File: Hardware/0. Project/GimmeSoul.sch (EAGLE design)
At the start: 24 parts, among them CN1 2.1MMJACKTHM, U1 ATMEGA328P-AU, U2 REG1117-5.0

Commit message: Jumpers on PCB layout bug fix
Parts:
- added SJ2: (no value), jumper:SJ
- SJ1: device jumper:SJ2W -> jumper:SJ
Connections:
- new net N$6: JP1.3, SJ1.2
- net +5V: no longer JP1.2
- net ICSP_RESET: now also SJ2.1; no longer SJ1.3
- net N$5: now also SJ2.2; no longer SJ1.2
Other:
- note added: "DC Power Jack J4"
- note added: "On the first use of the GimmeSoul (U1 bootloader programing): SJ1 = OPEN SJ2 = CLOSE After, SJ1 = CLOSE SJ2 = OPEN"
- note removed: "SJ1 - Position 2-1: Position for conventional use of GimmeSoul. This position allows you to standalone programming the bootloader of other ATmega."
- note removed: "SJ1 - Position 2-3: On the first use of the GimmeSoul, this position allows you to programming the U1 bootloader using an Arduino UNO."
- moved on the sheet: CN1

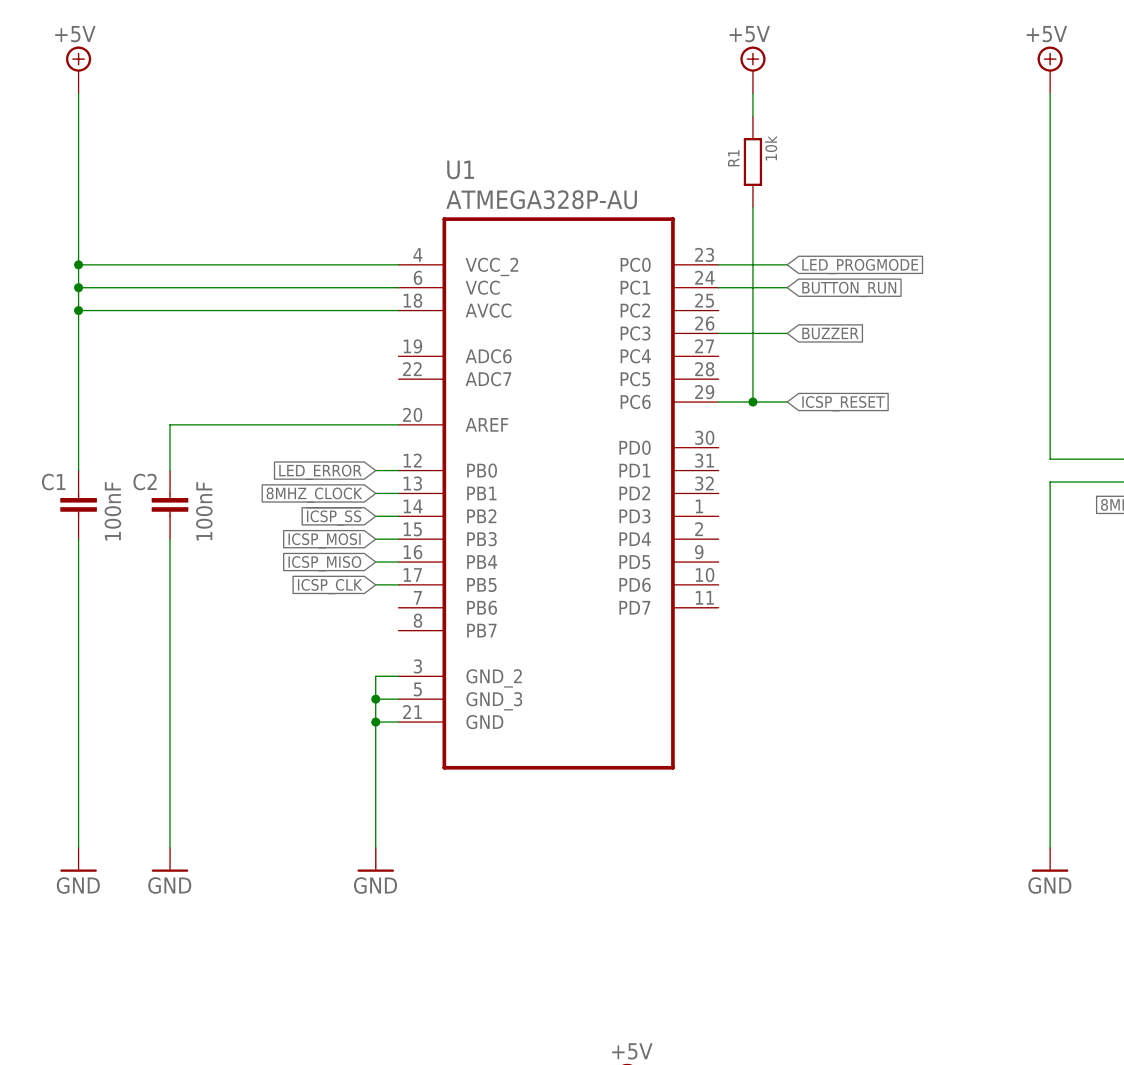
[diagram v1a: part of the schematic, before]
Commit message: 16MHz crystal added to MCU
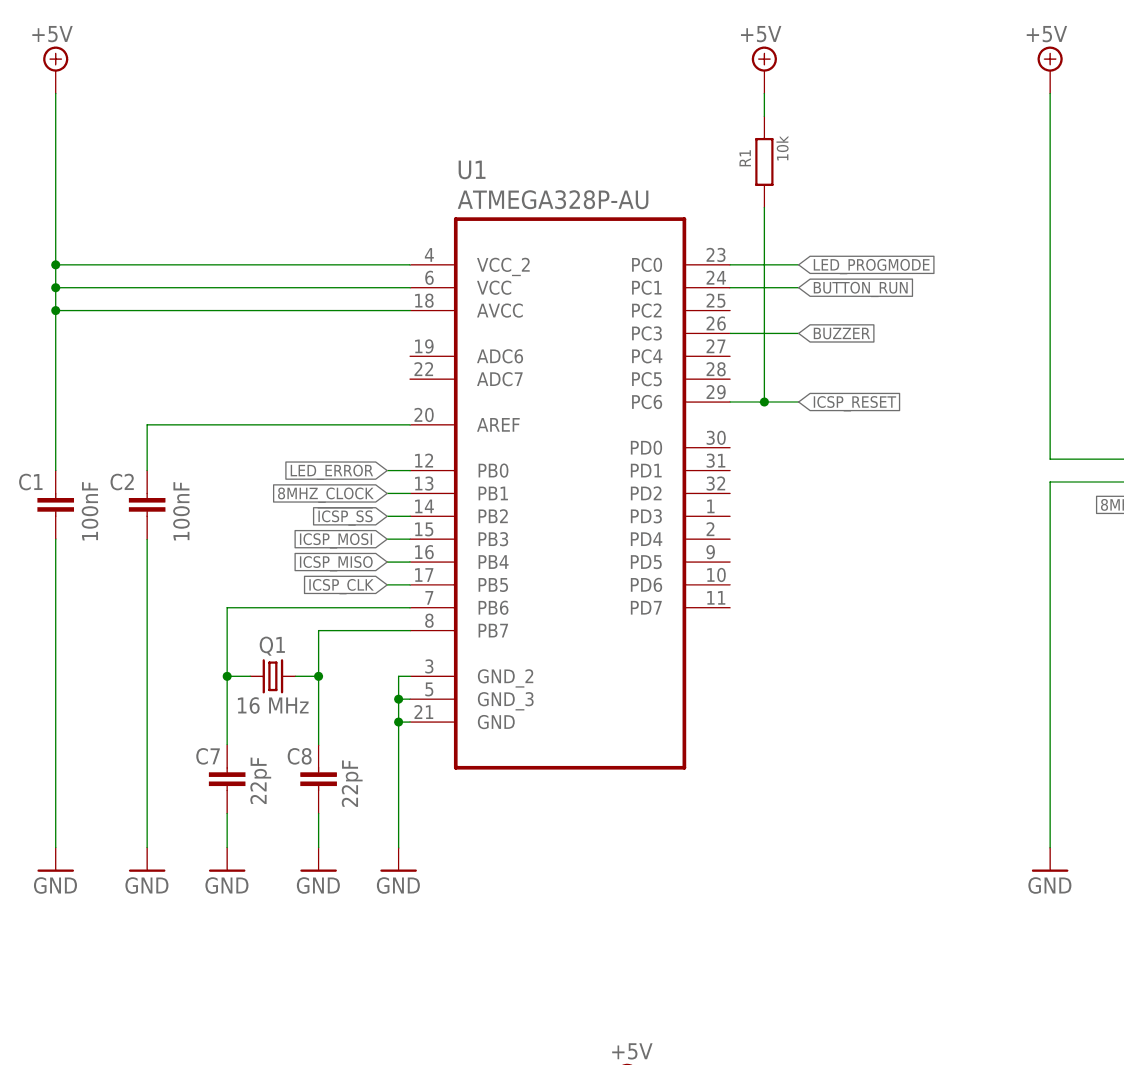
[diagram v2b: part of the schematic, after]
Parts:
- added C7, C8: 22pF, rcl:C-EUC0805
- added Q1: 16 MHz, crystal:CRYSTALHC49S
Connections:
- new net N$7: C7.2, Q1.1, U1.PB6
- new net N$8: C8.2, Q1.2, U1.PB7
- net GND: now also C7.1, C8.1
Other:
- moved on the sheet: C1, C2, R1, U1

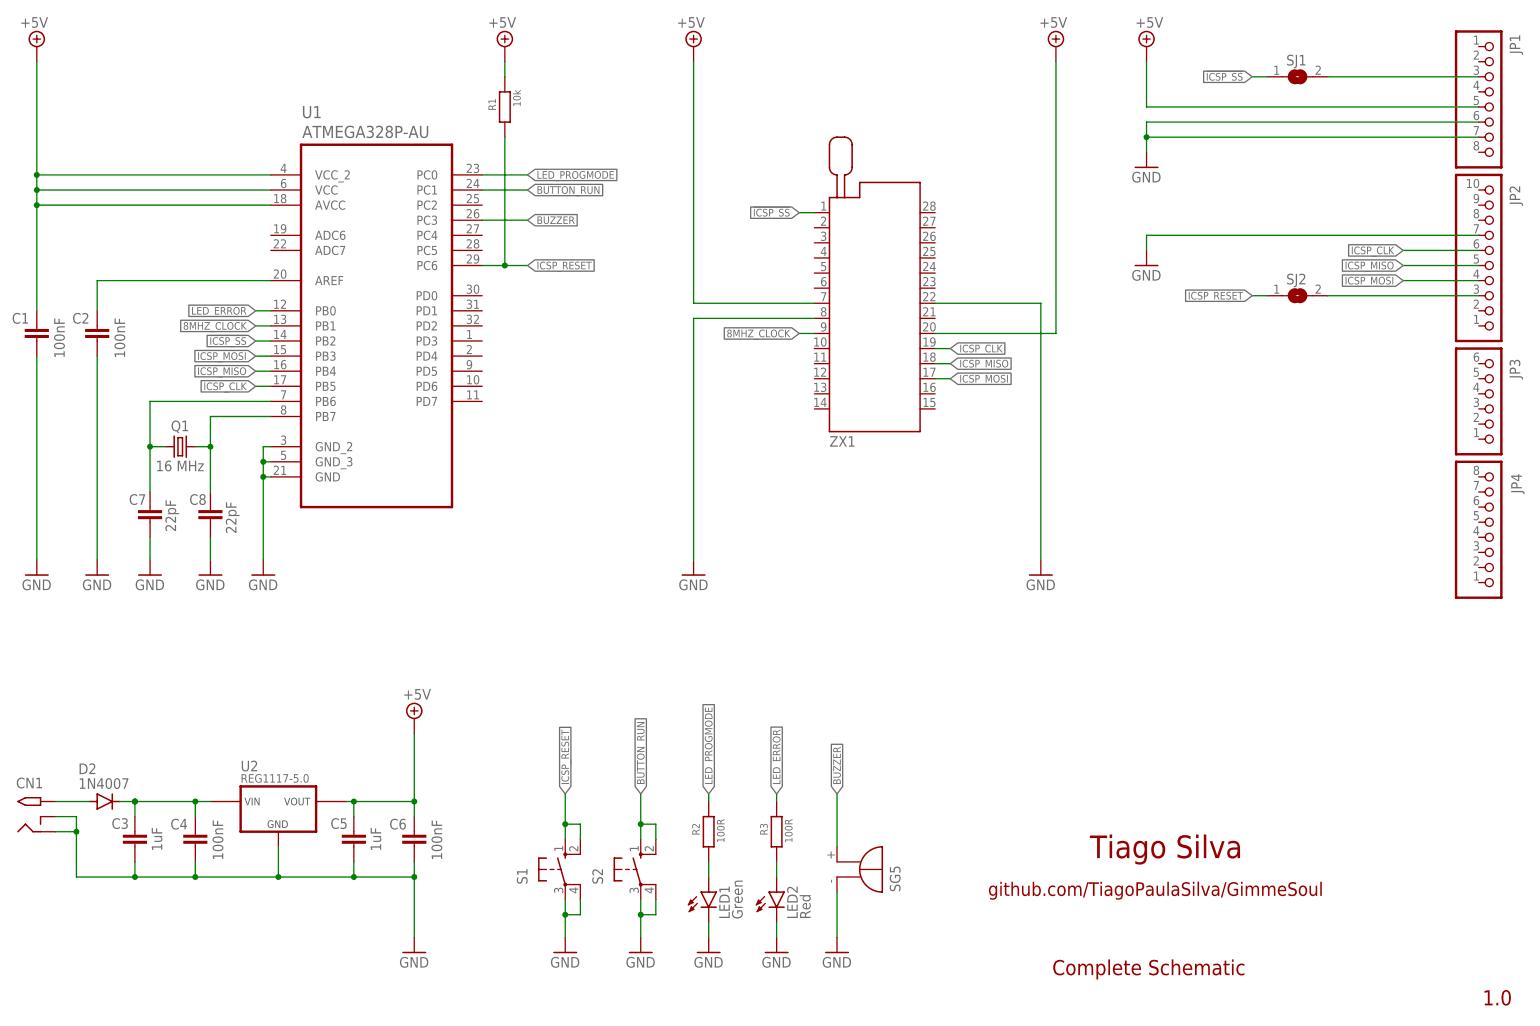
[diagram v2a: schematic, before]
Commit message: Silk Screen ref generated
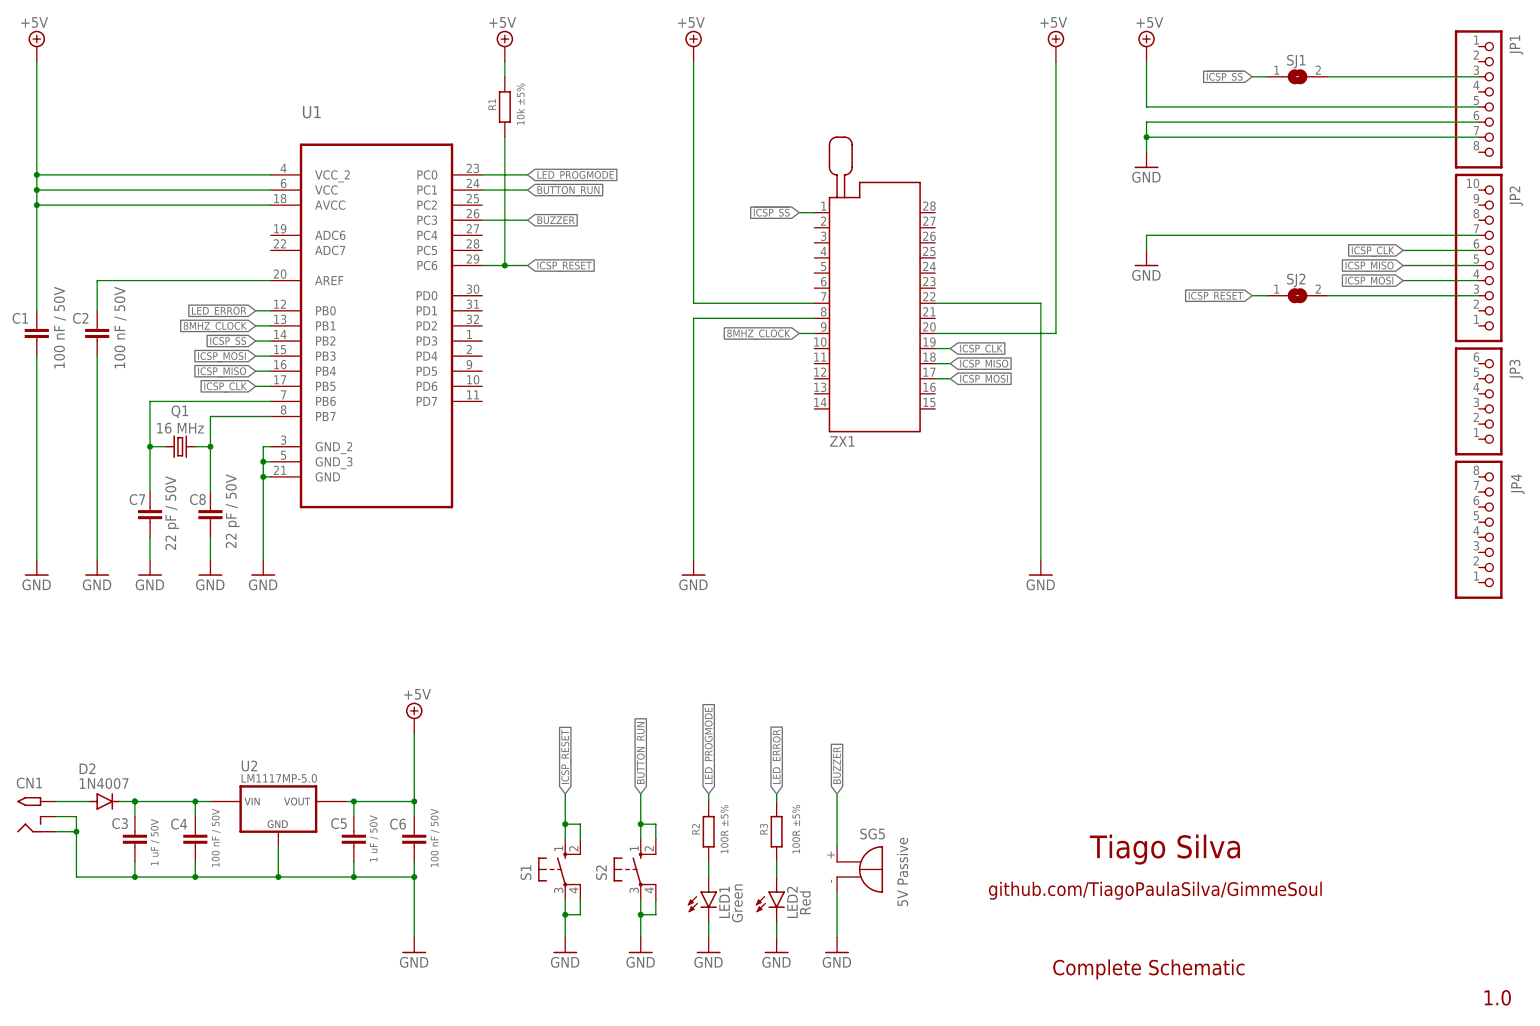
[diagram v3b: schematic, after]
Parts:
- C1, C2, C4, C6: value 100nF -> 100 nF / 50V
- C3, C5: value 1uF -> 1 uF / 50V
- C7, C8: value 22pF -> 22 pF / 50V
- R1: value 10k -> 10k ±5%
- R2, R3: value 100R -> 100R ±5%
- SG5: value 5V PASSIVE -> 5V Passive
- U2: value REG1117-5.0 -> LM1117MP-5.0
